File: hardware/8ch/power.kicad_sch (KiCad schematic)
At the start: 23 parts, among them J1 24V_INPUT, U14 LM5164DDAR

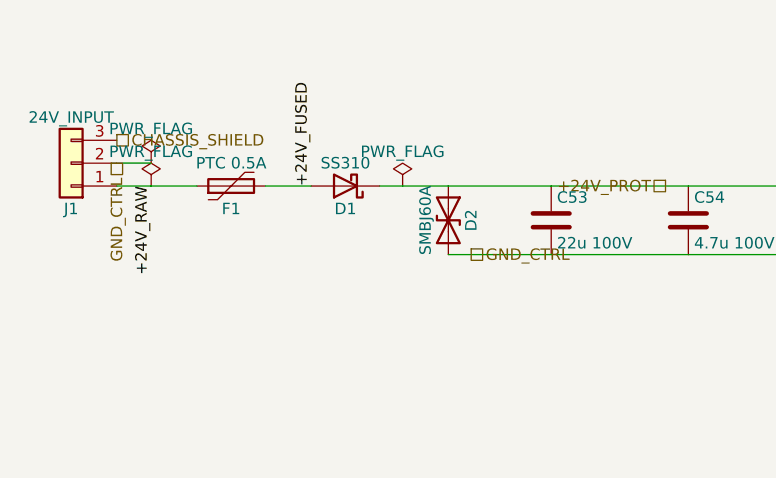
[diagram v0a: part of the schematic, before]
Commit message: REV A2: pre-fabrication fixes I-065..I-069 (decision 0022)
- U10/U11 ISO7760DWR/ISO7761DWR (no F: open input -> HIGH) + R61 2k2 on
  U11 OUTF -> MISO_CTRL so in-circuit ISP works (I-065)
- Q1 BSS131 240 V SOT-23 replaces the 60 V 2N7000 (I-066)
- R53/R54 100k/22k: 0.28 mA into PC2's clamp at 58 V (I-067)
- F1 1812L075/60GR, 60 V 0.75 A 1812 (I-068)
- D2 drawn unidirectional, D3 = M7 SMA, U12 sourcing warning (I-069)
- netlist-baseline-reva2.json (202/163/647), BOARD_REV A2
- board regenerated and re-routed; one hand via for C41.1 (+5V_CTRL)
- run_all.ps1 no longer calls populate_schematic.py (hierarchical sheet)

validate.ps1 2026-09-28 01:07: ERC 0/0, netlist IDENTICAL, DRC 0/0/0/0;
check_board.py all 6 ok; firmware build + 3 suites pass.

Co-Authored-By: Claude Opus 5.5 <noreply@anthropic.com>
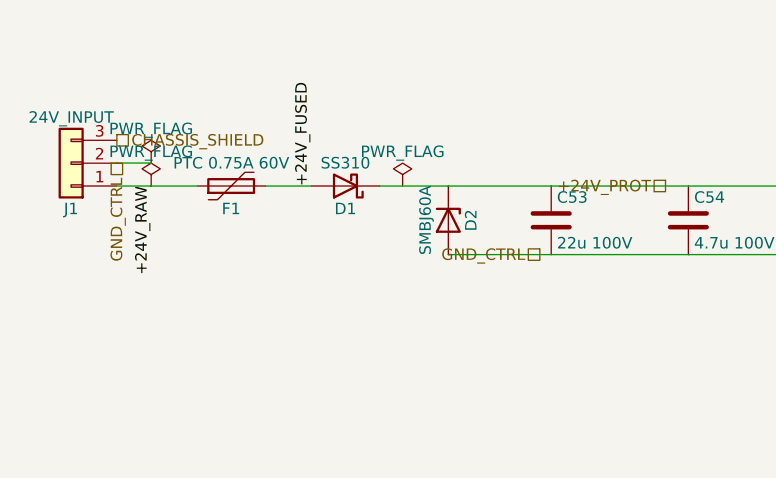
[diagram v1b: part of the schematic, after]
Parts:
- D2: symbol Device:D_TVS -> Device:D_Zener; Manufacturer MDD -> R+O
- F1: value PTC 0.5A -> PTC 0.75A 60V; footprint Fuse:Fuse_1206_3216Metric -> Fuse:Fuse_1812_4532Metric; LCSC C2982267 -> C48985874; MPN ASMD1206-050-30V -> 1812L075/60GR; Manufacturer Yageo -> LUTE
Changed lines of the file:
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@@
 	(hierarchical_label "GND_CTRL"
 		(shape passive)
-		(at 78.74 93.98 0)
+		(at 86.36 93.98 180)
 		(effects
 			(font
 				(size 1.27 1.27)
 			)
-			(justify left bottom)
+			(justify right bottom)
 		)
 	)
@@
 	)
 	(symbol
-		(lib_id "Device:D_TVS")
+		(lib_id "Device:D_Zener")
 		(at 76.2 90.17 270)
 		(unit 1)
@@
 			)
 		)
-		(property "Manufacturer" "MDD"
+		(property "Manufacturer" "R+O"
 			(at 76.2 90.17 0)
 			(hide yes)
@@
 			)
 		)
-		(property "Value" "PTC 0.5A"
+		(property "Value" "PTC 0.75A 60V"
 			(at 52.07 83.82 90)
 			(show_name no)
@@
 			)
 		)
-		(property "Footprint" "Fuse:Fuse_1206_3216Metric"
+		(property "Footprint" "Fuse:Fuse_1812_4532Metric"
 			(at 53.34 81.28 0)
 			(hide yes)
@@
 			)
 		)
-		(property "Datasheet" ""
+		(property "Datasheet" "../../docs/reference/datasheets/1812L-PTC.pdf"
 			(at 52.07 86.36 0)
 			(hide yes)
@@
 			)
 		)
-		(property "Description" "Resettable input over-current protection"
+		(property "Description" "Resettable input over-current protection, 60 V rated (I-068); the panel fuse of decision 0020 breaks battery shorts"
 			(at 52.07 86.36 0)
 			(hide yes)
@@
 			)
 		)
-		(property "MPN" "ASMD1206-050-30V"
+		(property "MPN" "1812L075/60GR"
 			(at 52.07 86.36 0)
 			(hide yes)
@@
 			)
 		)
-		(property "Manufacturer" "Yageo"
+		(property "Manufacturer" "LUTE"
 			(at 52.07 86.36 0)
 			(hide yes)
@@
 			)
 		)
-		(property "LCSC" "C2982267"
+		(property "LCSC" "C48985874"
 			(at 52.07 86.36 0)
 			(hide yes)

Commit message: U14 thermal vias 0.3 mm (0023, supersedes 0017); C41.1 fixed via; REV A2 re-routed
Smallest hole on the board is now 0.3 mm. Board fully generated, no hand edits.
validate.ps1 2026-09-28 01:43: ERC 0/0, netlist IDENTICAL 202/163/647,
DRC 0/0/0/0; check_board.py all 6 ok.

Co-Authored-By: Claude Opus 5.5 <noreply@anthropic.com>
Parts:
- U14: footprint Package_SO:SOIC-8-1EP_3.9x4.9mm_P1.27mm_EP2.41x3.3mm_ThermalVias -> Package_SO:SOIC-8-1EP_3.9x4.9mm_P1.27mm_EP2.41x3.3mm
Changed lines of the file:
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@@
 			)
 		)
-		(property "Footprint" "Package_SO:SOIC-8-1EP_3.9x4.9mm_P1.27mm_EP2.41x3.3mm_ThermalVias"
+		(property "Footprint" "Package_SO:SOIC-8-1EP_3.9x4.9mm_P1.27mm_EP2.41x3.3mm"
 			(at 162.56 82.55 0)
 			(show_name no)

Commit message: Image guard refuses unapproved images (I-082); refused-ACK reason on LCD (I-088); every BOM line sourced (0027)
- program.ps1 exits 2 on any image but thermo_8ch_max31856.hex (run: legacy image -> exit 2, no avrdude)
- NO ACK CHn HOT/FAULT status after a refused ACK; permit logic unchanged
- LCSC codes: MAX31856MUD+T, LP2985, ADM2587E, ATmega32A-PU, 3296W
- substitutes: K1 G5LE-14 DC24, C53 Rubycon 100YXF22; U12 XP IA0505S from DigiKey
- technician fits THT; 3 boards
build.ps1 exit 0, 3 suites PASS; validate.ps1 01:25 ERC 0/0, IDENTICAL, DRC 0/0/0/0.

Co-Authored-By: Claude Opus 5.5 <noreply@anthropic.com>
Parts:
- C53: LCSC (none) -> C88838; MPN EEUFC2A220 -> 100YXF22MEFC8X11.5; Manufacturer Panasonic -> Rubycon
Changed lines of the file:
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@@
 			)
 		)
-		(property "MPN" "EEUFC2A220"
+		(property "MPN" "100YXF22MEFC8X11.5"
 			(at 87.63 90.17 0)
 			(hide yes)
@@
 			)
 		)
-		(property "Manufacturer" "Panasonic"
+		(property "Manufacturer" "Rubycon"
 			(at 87.63 90.17 0)
 			(hide yes)
@@
 			(effects
 				(font
+					(size 1.27 1.27)
+				)
+			)
+		)
+		(property "LCSC" "C88838"
+			(at 87.63 90.17 0)
+			(hide yes)
+			(effects
+				(font
